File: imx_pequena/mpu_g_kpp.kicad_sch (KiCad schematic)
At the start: 1 part, among them U1 MCIMX6Z0DVM09AB

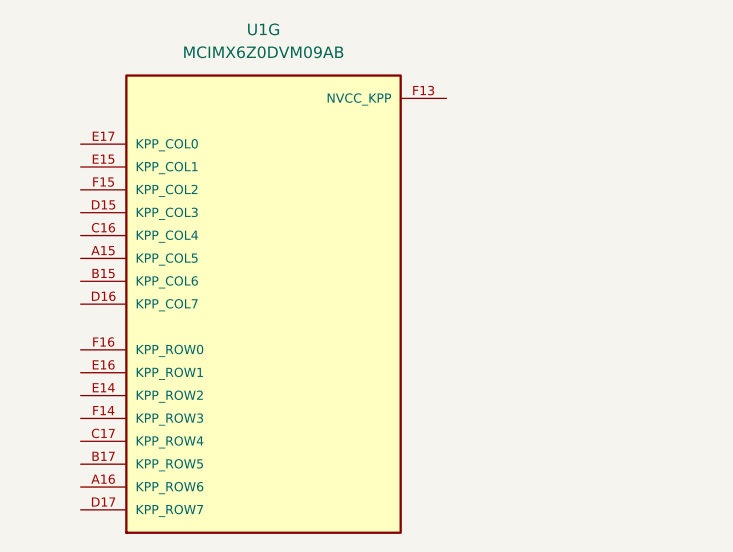
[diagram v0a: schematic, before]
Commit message: Cleaned up NVCC pins
Added 3v3 connections + decoupling caps to NVcc pins
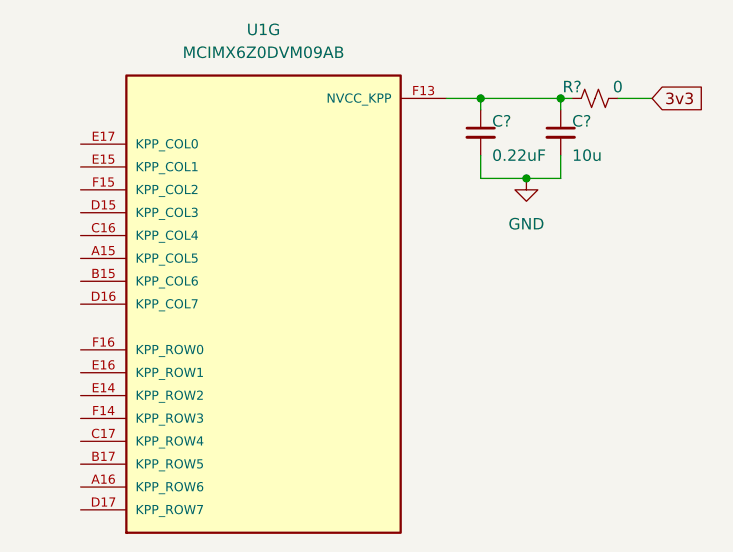
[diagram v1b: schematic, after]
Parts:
- added C?: 10u, symbol Device:C_Small
- added C?: 0.22uF, symbol Device:C_Small
- added R?: 0, symbol Device:R_Small_US
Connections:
- net at U1.F13 (NVCC_KPP): now also C?.1, C?.1, R?.1
- new net 3v3: R?.2
- new net GND: C?.2, C?.2
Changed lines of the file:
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@@
 (kicad_sch (version 20211123) (generator eeschema)
   (paper "A4")
+  (junction (at 179.07 77.47) (diameter 0) (color 0 0 0 0)
+  )
+  (junction (at 182.88 68.58) (diameter 0) (color 0 0 0 0)
+  )
+  (junction (at 173.99 68.58) (diameter 0) (color 0 0 0 0)
+  )
+  (wire (pts (xy 173.99 74.93) (xy 173.99 77.47))
+    (stroke (width 0) (type default) (color 0 0 0 0))
+  )
+  (wire (pts (xy 173.99 68.58) (xy 173.99 69.85))
+    (stroke (width 0) (type default) (color 0 0 0 0))
+  )
+  (wire (pts (xy 170.18 68.58) (xy 173.99 68.58))
+    (stroke (width 0) (type default) (color 0 0 0 0))
+  )
+  (wire (pts (xy 173.99 77.47) (xy 179.07 77.47))
+    (stroke (width 0) (type default) (color 0 0 0 0))
+  )
+  (wire (pts (xy 179.07 77.47) (xy 182.88 77.47))
+    (stroke (width 0) (type default) (color 0 0 0 0))
+  )
+  (wire (pts (xy 182.88 74.93) (xy 182.88 77.47))
+    (stroke (width 0) (type default) (color 0 0 0 0))
+  )
+  (wire (pts (xy 189.23 68.58) (xy 193.04 68.58))
+    (stroke (width 0) (type default) (color 0 0 0 0))
+  )
+  (wire (pts (xy 182.88 68.58) (xy 182.88 69.85))
+    (stroke (width 0) (type default) (color 0 0 0 0))
+  )
+  (wire (pts (xy 182.88 68.58) (xy 184.15 68.58))
+    (stroke (width 0) (type default) (color 0 0 0 0))
+  )
+  (wire (pts (xy 173.99 68.58) (xy 182.88 68.58))
+    (stroke (width 0) (type default) (color 0 0 0 0))
+  )
+  (global_label "3v3" (shape input) (at 193.04 68.58 0) (fields_autoplaced)
+    (effects (font (size 1.27 1.27)) (justify left))
+    (property "Intersheet References" "${INTERSHEET_REFS}" (id 0) (at 198.8398 68.5006 0)
+      (effects (font (size 1.27 1.27)) (justify left) hide)
+    )
+  )
   (symbol (lib_id "MCIMX6Z0DVM09AB:MCIMX6Z0DVM09AB") (at 149.86 91.44 0) (unit 7)
     (in_bom yes) (on_board yes) (fields_autoplaced)
@@
     (pin "F16")
   )
+  (symbol (lib_id "Device:C_Small") (at 182.88 72.39 0) (unit 1)
+    (in_bom yes) (on_board yes)
+    (property "Reference" "C?" (id 0) (at 184.15 71.12 0)
+      (effects (font (size 1.27 1.27)) (justify left))
+    )
+    (property "Value" "10u" (id 1) (at 184.15 74.93 0)
+      (effects (font (size 1.27 1.27)) (justify left))
+    )
+    (property "Footprint" "" (id 2) (at 182.88 72.39 0)
+      (effects (font (size 1.27 1.27)) hide)
+    )
+    (property "Datasheet" "~" (id 3) (at 182.88 72.39 0)
+      (effects (font (size 1.27 1.27)) hide)
+    )
+    (pin "1")
+    (pin "2")
+  )
+  (symbol (lib_id "Device:R_Small_US") (at 186.69 68.58 90) (unit 1)
+    (in_bom yes) (on_board yes)
+    (property "Reference" "R?" (id 0) (at 184.15 67.31 90))
+    (property "Value" "0" (id 1) (at 189.23 67.31 90))
+    (property "Footprint" "" (id 2) (at 186.69 68.58 0)
+      (effects (font (size 1.27 1.27)) hide)
+    )
+    (property "Datasheet" "~" (id 3) (at 186.69 68.58 0)
+      (effects (font (size 1.27 1.27)) hide)
+    )
+    (pin "1")
+    (pin "2")
+  )
+  (symbol (lib_id "Device:C_Small") (at 173.99 72.39 0) (unit 1)
+    (in_bom yes) (on_board yes)
+    (property "Reference" "C?" (id 0) (at 175.26 71.12 0)
+      (effects (font (size 1.27 1.27)) (justify left))
+    )
+    (property "Value" "0.22uF" (id 1) (at 175.26 74.93 0)
+      (effects (font (size 1.27 1.27)) (justify left))
+    )
+    (property "Footprint" "" (id 2) (at 173.99 72.39 0)
+      (effects (font (size 1.27 1.27)) hide)
+    )
+    (property "Datasheet" "~" (id 3) (at 173.99 72.39 0)
+      (effects (font (size 1.27 1.27)) hide)
+    )
+    (pin "1")
+    (pin "2")
+  )
+  (symbol (lib_id "power:GND") (at 179.07 77.47 0) (unit 1)
+    (in_bom yes) (on_board yes) (fields_autoplaced)
+    (property "Reference" "#PWR?" (id 0) (at 179.07 83.82 0)
+      (effects (font (size 1.27 1.27)) hide)
+    )
+    (property "Value" "GND" (id 1) (at 179.07 82.55 0))
+    (property "Footprint" "" (id 2) (at 179.07 77.47 0)
+      (effects (font (size 1.27 1.27)) hide)
+    )
+    (property "Datasheet" "" (id 3) (at 179.07 77.47 0)
+      (effects (font (size 1.27 1.27)) hide)
+    )
+    (pin "1")
+  )
 )

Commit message: Pinout updates
Updated pinout files, changed pinout of gpio 1 and 3
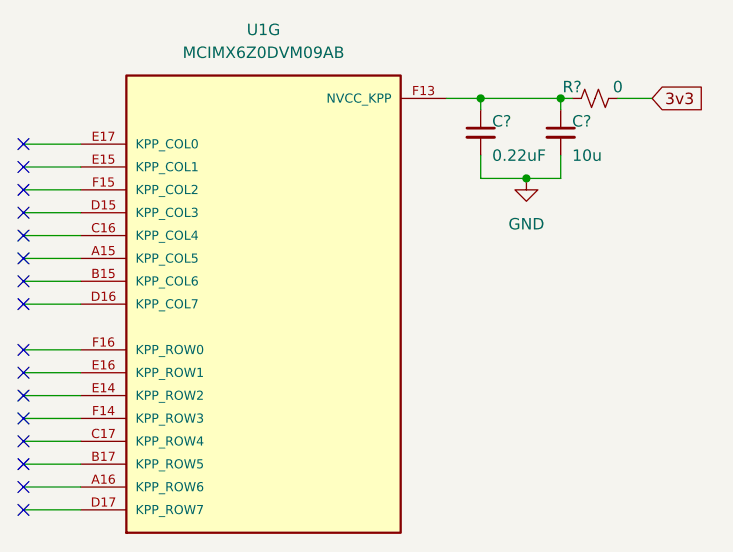
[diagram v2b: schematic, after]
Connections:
- no-connect marks 0 -> 16
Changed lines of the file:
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@@
   (junction (at 173.99 68.58) (diameter 0) (color 0 0 0 0)
   )
+  (no_connect (at 123.19 101.6))
+  (no_connect (at 123.19 91.44))
+  (no_connect (at 123.19 86.36))
+  (no_connect (at 123.19 88.9))
+  (no_connect (at 123.19 109.22))
+  (no_connect (at 123.19 111.76))
+  (no_connect (at 123.19 114.3))
+  (no_connect (at 123.19 83.82))
+  (no_connect (at 123.19 96.52))
+  (no_connect (at 123.19 81.28))
+  (no_connect (at 123.19 73.66))
+  (no_connect (at 123.19 76.2))
+  (no_connect (at 123.19 78.74))
+  (no_connect (at 123.19 104.14))
+  (no_connect (at 123.19 99.06))
+  (no_connect (at 123.19 106.68))
+  (wire (pts (xy 123.19 111.76) (xy 129.54 111.76))
+    (stroke (width 0) (type default) (color 0 0 0 0))
+  )
+  (wire (pts (xy 123.19 88.9) (xy 129.54 88.9))
+    (stroke (width 0) (type default) (color 0 0 0 0))
+  )
+  (wire (pts (xy 123.19 81.28) (xy 129.54 81.28))
+    (stroke (width 0) (type default) (color 0 0 0 0))
+  )
   (wire (pts (xy 173.99 74.93) (xy 173.99 77.47))
+    (stroke (width 0) (type default) (color 0 0 0 0))
+  )
+  (wire (pts (xy 123.19 78.74) (xy 129.54 78.74))
+    (stroke (width 0) (type default) (color 0 0 0 0))
+  )
+  (wire (pts (xy 123.19 73.66) (xy 129.54 73.66))
     (stroke (width 0) (type default) (color 0 0 0 0))
   )
@@
     (stroke (width 0) (type default) (color 0 0 0 0))
   )
+  (wire (pts (xy 123.19 109.22) (xy 129.54 109.22))
+    (stroke (width 0) (type default) (color 0 0 0 0))
+  )
   (wire (pts (xy 182.88 74.93) (xy 182.88 77.47))
+    (stroke (width 0) (type default) (color 0 0 0 0))
+  )
+  (wire (pts (xy 123.19 99.06) (xy 129.54 99.06))
+    (stroke (width 0) (type default) (color 0 0 0 0))
+  )
+  (wire (pts (xy 123.19 114.3) (xy 129.54 114.3))
+    (stroke (width 0) (type default) (color 0 0 0 0))
+  )
+  (wire (pts (xy 123.19 83.82) (xy 129.54 83.82))
+    (stroke (width 0) (type default) (color 0 0 0 0))
+  )
+  (wire (pts (xy 123.19 96.52) (xy 129.54 96.52))
+    (stroke (width 0) (type default) (color 0 0 0 0))
+  )
+  (wire (pts (xy 123.19 86.36) (xy 129.54 86.36))
     (stroke (width 0) (type default) (color 0 0 0 0))
   )
@@
     (stroke (width 0) (type default) (color 0 0 0 0))
   )
+  (wire (pts (xy 123.19 106.68) (xy 129.54 106.68))
+    (stroke (width 0) (type default) (color 0 0 0 0))
+  )
+  (wire (pts (xy 123.19 104.14) (xy 129.54 104.14))
+    (stroke (width 0) (type default) (color 0 0 0 0))
+  )
   (wire (pts (xy 182.88 68.58) (xy 182.88 69.85))
     (stroke (width 0) (type default) (color 0 0 0 0))
   )
+  (wire (pts (xy 123.19 91.44) (xy 129.54 91.44))
+    (stroke (width 0) (type default) (color 0 0 0 0))
+  )
+  (wire (pts (xy 123.19 76.2) (xy 129.54 76.2))
+    (stroke (width 0) (type default) (color 0 0 0 0))
+  )
+  (wire (pts (xy 123.19 101.6) (xy 129.54 101.6))
+    (stroke (width 0) (type default) (color 0 0 0 0))
+  )

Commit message: Part Assignment
Assigned GPIOs and assigned footprints to most parts
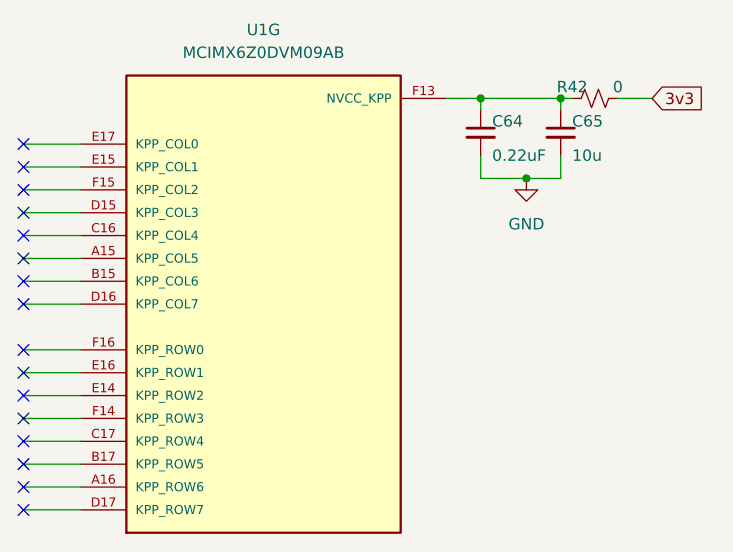
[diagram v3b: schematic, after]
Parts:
- C64: renamed from C?; footprint (none) -> Capacitor_SMD:C_0402_1005Metric
- C65: renamed from C?; footprint (none) -> Capacitor_SMD:C_0805_2012Metric
- R42: renamed from R?; footprint (none) -> Resistor_SMD:R_0402_1005Metric
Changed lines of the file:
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@@
   (symbol (lib_id "Device:C_Small") (at 182.88 72.39 0) (unit 1)
     (in_bom yes) (on_board yes)
-    (property "Reference" "C?" (id 0) (at 184.15 71.12 0)
+    (property "Reference" "C65" (id 0) (at 184.15 71.12 0)
       (effects (font (size 1.27 1.27)) (justify left))
     )
@@
       (effects (font (size 1.27 1.27)) (justify left))
     )
-    (property "Footprint" "" (id 2) (at 182.88 72.39 0)
+    (property "Footprint" "Capacitor_SMD:C_0805_2012Metric" (id 2) (at 182.88 72.39 0)
       (effects (font (size 1.27 1.27)) hide)
     )
@@
   (symbol (lib_id "Device:R_Small_US") (at 186.69 68.58 90) (unit 1)
     (in_bom yes) (on_board yes)
-    (property "Reference" "R?" (id 0) (at 184.15 67.31 90))
+    (property "Reference" "R42" (id 0) (at 184.15 67.31 90))
     (property "Value" "0" (id 1) (at 189.23 67.31 90))
-    (property "Footprint" "" (id 2) (at 186.69 68.58 0)
+    (property "Footprint" "Resistor_SMD:R_0402_1005Metric" (id 2) (at 186.69 68.58 0)
       (effects (font (size 1.27 1.27)) hide)
     )
@@
   (symbol (lib_id "Device:C_Small") (at 173.99 72.39 0) (unit 1)
     (in_bom yes) (on_board yes)
-    (property "Reference" "C?" (id 0) (at 175.26 71.12 0)
+    (property "Reference" "C64" (id 0) (at 175.26 71.12 0)
       (effects (font (size 1.27 1.27)) (justify left))
     )
@@
       (effects (font (size 1.27 1.27)) (justify left))
     )
-    (property "Footprint" "" (id 2) (at 173.99 72.39 0)
+    (property "Footprint" "Capacitor_SMD:C_0402_1005Metric" (id 2) (at 173.99 72.39 0)
       (effects (font (size 1.27 1.27)) hide)
     )
@@
   (symbol (lib_id "power:GND") (at 179.07 77.47 0) (unit 1)
     (in_bom yes) (on_board yes) (fields_autoplaced)
-    (property "Reference" "#PWR?" (id 0) (at 179.07 83.82 0)
+    (property "Reference" "#PWR0154" (id 0) (at 179.07 83.82 0)
       (effects (font (size 1.27 1.27)) hide)
     )
